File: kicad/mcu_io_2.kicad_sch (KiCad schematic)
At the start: 4 parts, among them U7 MCXN947VDFT, Y2 32.768kHz

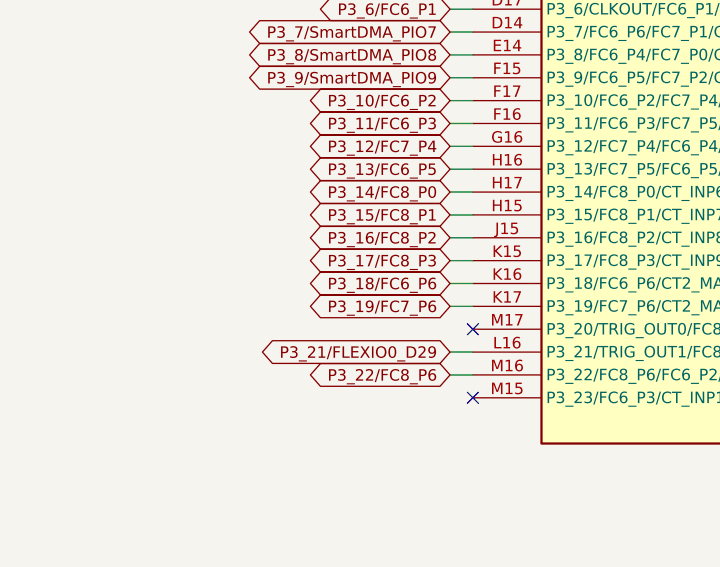
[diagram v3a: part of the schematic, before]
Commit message: Updated schematic after feedback from Jari
- Finished schematic after feedback from Jari. It is at a finished state, can be reviewed by whole team now.
- Layouted MCXN with decoupling caps.
- Layouted Base100-T1 ethernet phy.
- Layouted the power supply a bit.
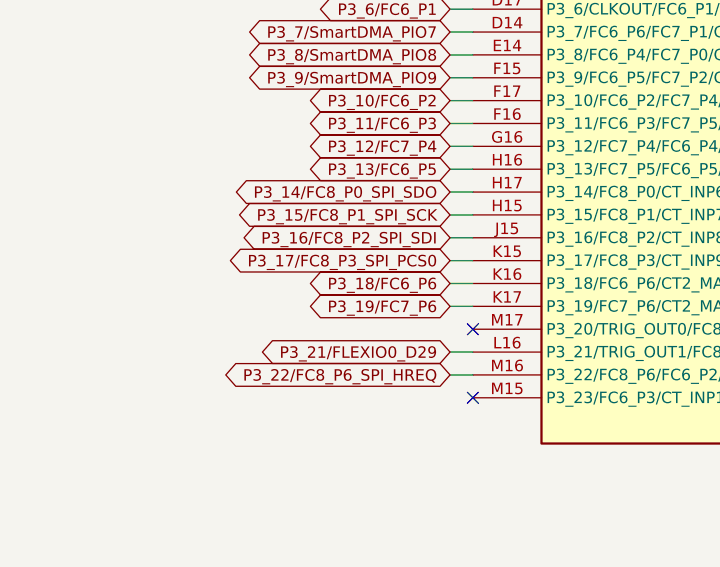
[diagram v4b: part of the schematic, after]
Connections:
- net P3_14/FC8_P0 renamed P3_14/FC8_P0_SPI_SDO
- net P3_15/FC8_P1 renamed P3_15/FC8_P1_SPI_SCK
- net P3_16/FC8_P2 renamed P3_16/FC8_P2_SPI_SDI
- net P3_17/FC8_P3 renamed P3_17/FC8_P3_SPI_PCS0
- net P3_22/FC8_P6 renamed P3_22/FC8_P6_SPI_HREQ
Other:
- title: MR-MCXN-T1 Sensor hub -> MR-MCXN-T1 Sensor Node
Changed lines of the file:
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@@
 	(paper "A3")
 	(title_block
-		(title "MR-MCXN-T1 Sensor hub")
-		(date "2025-03-20")
+		(title "MR-MCXN-T1 Sensor Node")
+		(date "2025-03-28")
 		(rev "X0")
 		(company "NXP SEMICONDUCTORS B.V.")
@@
 		)
 	)
-	(global_label "P3_15{slash}FC8_P1"
+	(global_label "P3_15{slash}FC8_P1_SPI_SCK"
 		(shape bidirectional)
 		(at 107.95 63.5 180)
@@
 		)
 		(property "Intersheetrefs" "${INTERSHEET_REFS}"
-			(at 89.6417 63.5 0)
+			(at 80.8727 63.5 0)
 			(effects
 				(font
@@
 		)
 	)
-	(global_label "P3_16{slash}FC8_P2"
+	(global_label "P3_16{slash}FC8_P2_SPI_SDI"
 		(shape bidirectional)
 		(at 107.95 66.04 180)
@@
 		)
 		(property "Intersheetrefs" "${INTERSHEET_REFS}"
-			(at 89.6417 66.04 0)
+			(at 81.5379 66.04 0)
 			(effects
 				(font
@@
 		)
 	)
-	(global_label "P3_14{slash}FC8_P0"
+	(global_label "P3_14{slash}FC8_P0_SPI_SDO"
 		(shape bidirectional)
 		(at 107.95 60.96 180)
@@
 		)
 		(property "Intersheetrefs" "${INTERSHEET_REFS}"
-			(at 89.6417 60.96 0)
+			(at 80.8122 60.96 0)
 			(effects
 				(font
@@
 		)
 	)
-	(global_label "P3_17{slash}FC8_P3"
+	(global_label "P3_17{slash}FC8_P3_SPI_PCS0"
 		(shape bidirectional)
 		(at 107.95 68.58 180)
@@
 		)
 		(property "Intersheetrefs" "${INTERSHEET_REFS}"
-			(at 89.6417 68.58 0)
+			(at 79.6632 68.58 0)
 			(effects
 				(font
@@
 		)
 	)
-	(global_label "P3_22{slash}FC8_P6"
+	(global_label "P3_22{slash}FC8_P6_SPI_HREQ"
 		(shape bidirectional)
 		(at 107.95 81.28 180)
@@
 		)
 		(property "Intersheetrefs" "${INTERSHEET_REFS}"
-			(at 89.6417 81.28 0)
-			(effects
-				(font
+			(at 79.5422 81.28 0)
+			(effects
+				(font

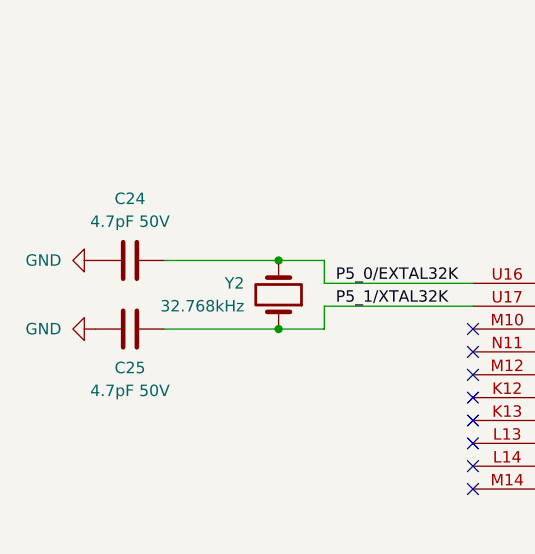
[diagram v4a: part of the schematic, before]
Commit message: Finished schematic. Completed power and ENET phy layout.
Layouted power supply and ethernet phy around input connector.
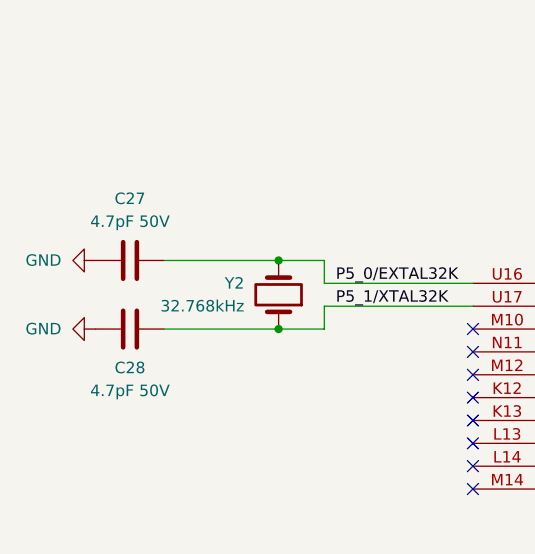
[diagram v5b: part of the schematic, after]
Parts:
- renumbered C24 to C27, C25 to C28
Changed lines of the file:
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@@
 		(on_board yes)
 		(dnp no)
-		(property "Reference" "C24"
+		(property "Reference" "C27"
 			(at 72.39 209.042 90)
 			(effects
@@
 			(project ""
 				(path "/8b469ec1-e800-4d46-8a32-95d77ceae6db/4619e5be-1f0d-457d-96e5-6e6d95033c83"
-					(reference "C24")
+					(reference "C27")
 					(unit 1)
 				)
@@
 		(dnp no)
 		(fields_autoplaced yes)
-		(property "Reference" "#PWR056"
+		(property "Reference" "#PWR057"
 			(at 62.23 223.52 0)
 			(effects
@@
 			(project ""
 				(path "/8b469ec1-e800-4d46-8a32-95d77ceae6db/4619e5be-1f0d-457d-96e5-6e6d95033c83"
-					(reference "#PWR056")
+					(reference "#PWR057")
 					(unit 1)
 				)
@@
 		(on_board yes)
 		(dnp no)
-		(property "Reference" "C25"
+		(property "Reference" "C28"
 			(at 72.39 227.838 90)
 			(effects
@@
 			(project ""
 				(path "/8b469ec1-e800-4d46-8a32-95d77ceae6db/4619e5be-1f0d-457d-96e5-6e6d95033c83"
-					(reference "C25")
+					(reference "C28")
 					(unit 1)
 				)
@@
 		(dnp no)
 		(fields_autoplaced yes)
-		(property "Reference" "#PWR055"
+		(property "Reference" "#PWR056"
 			(at 62.23 215.9 0)
 			(effects
@@
 			(project ""
 				(path "/8b469ec1-e800-4d46-8a32-95d77ceae6db/4619e5be-1f0d-457d-96e5-6e6d95033c83"
-					(reference "#PWR055")
+					(reference "#PWR056")
 					(unit 1)
 				)

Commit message: Updated layout and BOM
- Flipped Magnetometer so it is aligned with the axis of the IMU.
- Updated BOM so all parts can be sourced from DigiKey. Also added a row for JLCPCB part numbers if applicable.
- Replaced ISP button with the NanoT160AS. Added "ISP" in silkscreen at that button.
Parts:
- C27, C28: DigiKey (none) -> 490-8102-1-ND; JLCPCB (none) -> C161327; Supplier JLCPCB -> (none); Supplier PN C161327 -> (none)
- U7: DigiKey (none) -> 568-MCXN947VDFT-ND; JLCPCB (none) -> -; Supplier DigiKey -> (none); Supplier PN 568-MCXN947VDFT-ND -> (none)
- Y2: DigiKey (none) -> 732-830009678CT-ND; JLCPCB (none) -> -; Supplier DigiKey -> (none); Supplier PN 732-830009678CT-ND -> (none)
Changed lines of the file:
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@@
 			)
 		)
-		(property "Supplier" "JLCPCB"
+		(property "JLCPCB" "C161327"
 			(at 72.39 215.9 0)
 			(effects
@@
 			)
 		)
-		(property "Supplier PN" "C161327"
-			(at 72.39 215.9 0)
-			(effects
-				(font
-					(size 1.27 1.27)
-				)
-				(hide yes)
-			)
-		)
-		(property "MANUFACTURER" ""
-			(at 72.39 215.9 0)
-			(effects
-				(font
-					(size 1.27 1.27)
-				)
-				(hide yes)
-			)
-		)
-		(property "MAXIMUM_PACKAGE_HEIGHT" ""
-			(at 72.39 215.9 0)
-			(effects
-				(font
-					(size 1.27 1.27)
-				)
-				(hide yes)
-			)
-		)
-		(property "PARTREV" ""
-			(at 72.39 215.9 0)
-			(effects
-				(font
-					(size 1.27 1.27)
-				)
-				(hide yes)
-			)
-		)
-		(property "STANDARD" ""
+		(property "DigiKey" "490-8102-1-ND "
 			(at 72.39 215.9 0)
 			(effects
@@
 			)
 		)
-		(property "Supplier" "DigiKey"
+		(property "DigiKey" "732-830009678CT-ND"
 			(at 88.9 219.71 0)
 			(effects
@@
 			)
 		)
-		(property "Supplier PN" "732-830009678CT-ND"
-			(at 88.9 219.71 0)
-			(effects
-				(font
-					(size 1.27 1.27)
-				)
-				(hide yes)
-			)
-		)
-		(property "MANUFACTURER" ""
-			(at 88.9 219.71 0)
-			(effects
-				(font
-					(size 1.27 1.27)
-				)
-				(hide yes)
-			)
-		)
-		(property "MAXIMUM_PACKAGE_HEIGHT" ""
-			(at 88.9 219.71 0)
-			(effects
-				(font
-					(size 1.27 1.27)
-				)
-				(hide yes)
-			)
-		)
-		(property "PARTREV" ""
-			(at 88.9 219.71 0)
-			(effects
-				(font
-					(size 1.27 1.27)
-				)
-				(hide yes)
-			)
-		)
-		(property "STANDARD" ""
+		(property "JLCPCB" "-"
 			(at 88.9 219.71 0)
 			(effects
@@
 			)
 		)
-		(property "Supplier" "DigiKey"
+		(property "DigiKey" "568-MCXN947VDFT-ND"
 			(at 118.11 123.19 0)
 			(effects
@@
 			)
 		)
-		(property "Supplier PN" "568-MCXN947VDFT-ND"
-			(at 118.11 123.19 0)
-			(effects
-				(font
-					(size 1.27 1.27)
-				)
-				(hide yes)
-			)
-		)
-		(property "MANUFACTURER" ""
-			(at 118.11 123.19 0)
-			(effects
-				(font
-					(size 1.27 1.27)
-				)
-				(hide yes)
-			)
-		)
-		(property "MAXIMUM_PACKAGE_HEIGHT" ""
-			(at 118.11 123.19 0)
-			(effects
-				(font
-					(size 1.27 1.27)
-				)
-				(hide yes)
-			)
-		)
-		(property "PARTREV" ""
-			(at 118.11 123.19 0)
-			(effects
-				(font
-					(size 1.27 1.27)
-				)
-				(hide yes)
-			)
-		)
-		(property "STANDARD" ""
+		(property "JLCPCB" "-"
 			(at 118.11 123.19 0)
 			(effects
@@
 			)
 		)
-		(property "Supplier" "DigiKey"
+		(property "DigiKey" "568-MCXN947VDFT-ND"
 			(at 118.11 22.86 0)
 			(effects
@@
 			)
 		)
-		(property "Supplier PN" "568-MCXN947VDFT-ND"
-			(at 118.11 22.86 0)
-			(effects
-				(font
-					(size 1.27 1.27)
-				)
-				(hide yes)
-			)
-		)
-		(property "MANUFACTURER" ""
-			(at 118.11 22.86 0)
-			(effects
-				(font
-					(size 1.27 1.27)
-				)
-				(hide yes)
-			)
-		)
-		(property "MAXIMUM_PACKAGE_HEIGHT" ""
-			(at 118.11 22.86 0)
-			(effects
-				(font
-					(size 1.27 1.27)
-				)
-				(hide yes)
-			)
-		)
-		(property "PARTREV" ""
-			(at 118.11 22.86 0)
-			(effects
-				(font
-					(size 1.27 1.27)
-				)
-				(hide yes)
-			)
-		)
-		(property "STANDARD" ""
+		(property "JLCPCB" "-"
 			(at 118.11 22.86 0)
 			(effects
@@
 			)
 		)
-		(property "Supplier" "JLCPCB"
+		(property "JLCPCB" "C161327"
 			(at 72.39 223.52 0)
 			(effects
@@
 			)
 		)
-		(property "Supplier PN" "C161327"
-			(at 72.39 223.52 0)
-			(effects
-				(font
-					(size 1.27 1.27)
-				)
-				(hide yes)
-			)
-		)
-		(property "MANUFACTURER" ""
-			(at 72.39 223.52 0)
-			(effects
-				(font
-					(size 1.27 1.27)
-				)
-				(hide yes)
-			)
-		)
-		(property "MAXIMUM_PACKAGE_HEIGHT" ""
-			(at 72.39 223.52 0)
-			(effects
-				(font
-					(size 1.27 1.27)
-				)
-				(hide yes)
-			)
-		)
-		(property "PARTREV" ""
-			(at 72.39 223.52 0)
-			(effects
-				(font
-					(size 1.27 1.27)
-				)
-				(hide yes)
-			)
-		)
-		(property "STANDARD" ""
+		(property "DigiKey" "490-8102-1-ND "
 			(at 72.39 223.52 0)
 			(effects
@@
 			)
 		)
-		(property "Supplier" "DigiKey"
+		(property "DigiKey" "568-MCXN947VDFT-ND"
 			(at 118.11 213.36 0)
 			(effects
@@
 			)
 		)
-		(property "Supplier PN" "568-MCXN947VDFT-ND"
+		(property "JLCPCB" "-"
 			(at 118.11 213.36 0)
 			(effects
-				(font
-					(size 1.27 1.27)
-				)
-				(hide yes)
-			)
-		)
-		(property "MANUFACTURER" ""
-			(at 118.11 213.36 0)
-			(effects
-				(font
-					(size 1.27 1.27)
-				)
-				(hide yes)
-			)
-		)
-		(property "MAXIMUM_PACKAGE_HEIGHT" ""
-			(at 118.11 213.36 0)
-			(effects
-				(font
-					(size 1.27 1.27)
-				)
-				(hide yes)
-			)
-		)
-		(property "PARTREV" ""
-			(at 118.11 213.36 0)
-			(effects
-				(font
-					(size 1.27 1.27)
-				)
-				(hide yes)
-			)
-		)
-		(property "STANDARD" ""
-			(at 118.11 213.36 0)
-			(effects

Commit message: Update repo naming and cleanup files.
Signed-off-by: Benjamin Perseghetti <bperseghetti@rudislabs.com>
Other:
- title: MR-MCXN-T1 Sensor Node -> MR-MCXN-T1
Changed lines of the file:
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@@
 	(paper "A3")
 	(title_block
-		(title "MR-MCXN-T1 Sensor Node")
+		(title "MR-MCXN-T1")
 		(date "2025-03-28")
 		(rev "X0")
 		(company "NXP SEMICONDUCTORS B.V.")
-		(comment 1 "CLASSIFICATION: INTERNAL USE ONLY")
 		(comment 3 "DESIGNER: YOURI TILS")
 		(comment 4 "CTO SYSTEM INNOVATIONS / MOBILE ROBOTICS DOMAIN")
